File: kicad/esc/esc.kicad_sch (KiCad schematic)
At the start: 33 parts, among them Q1 IRF540N, Q2 IRF540N, Q3 IRF540N, Q4 IRF540N, Q5 IRF540N, Q6 IRF540N, U1 IR2110, U2 IR2110, U3 IR2110

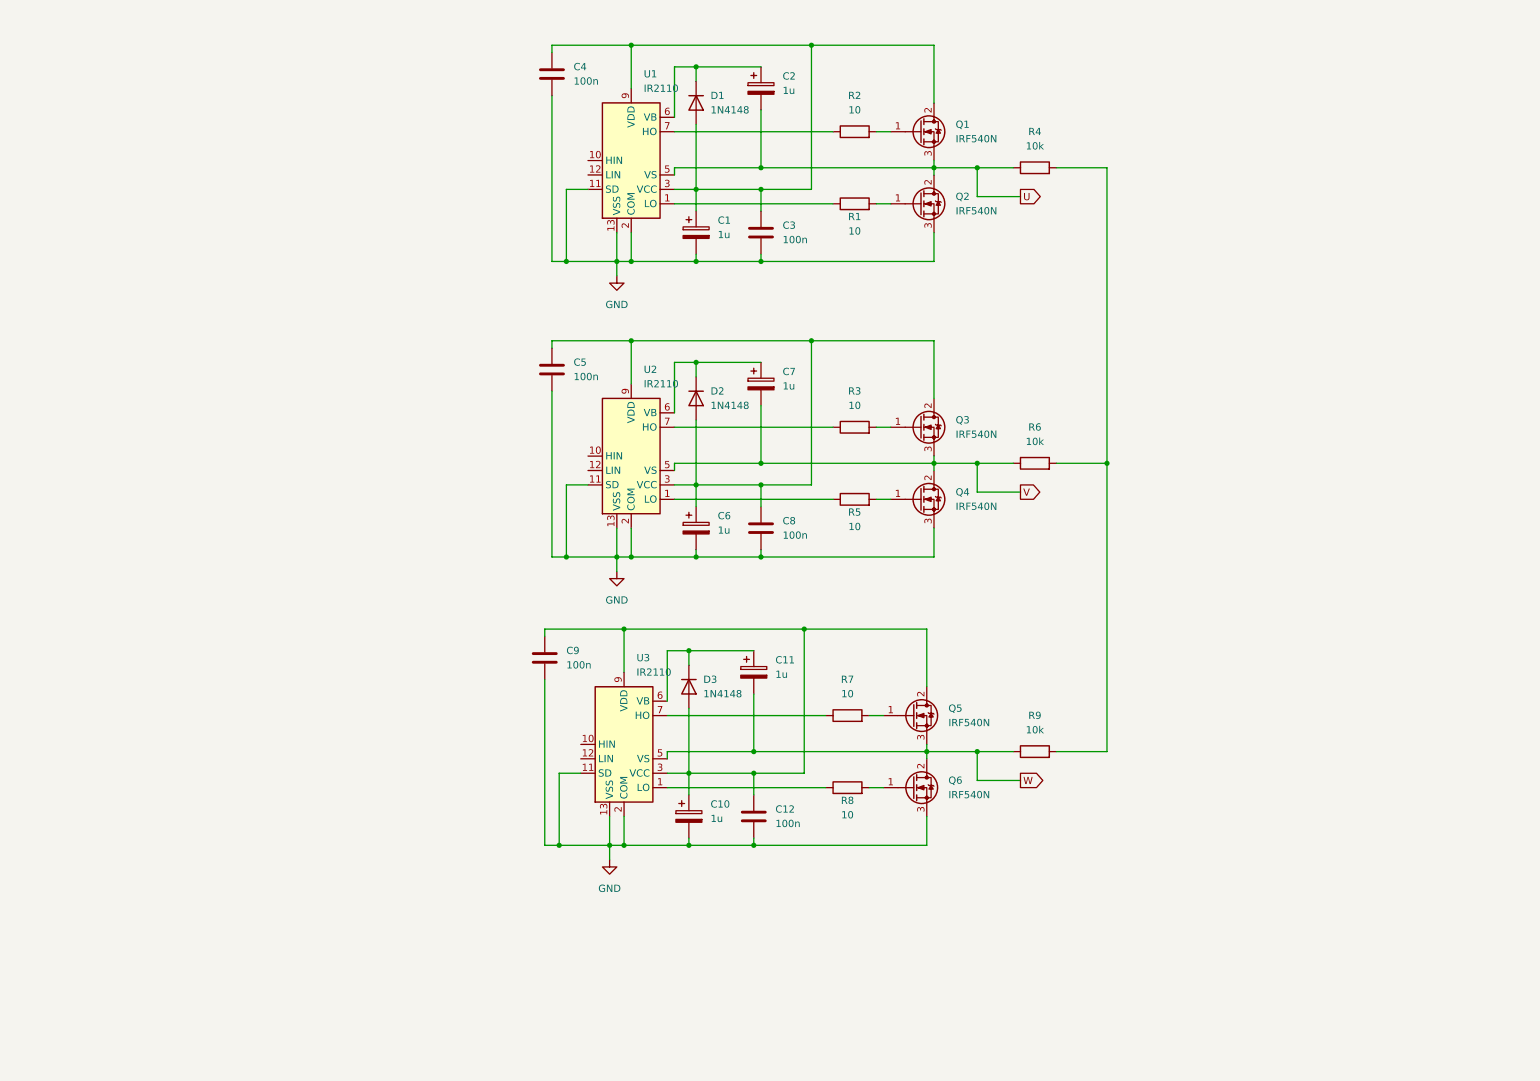
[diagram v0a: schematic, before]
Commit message: Added driver board
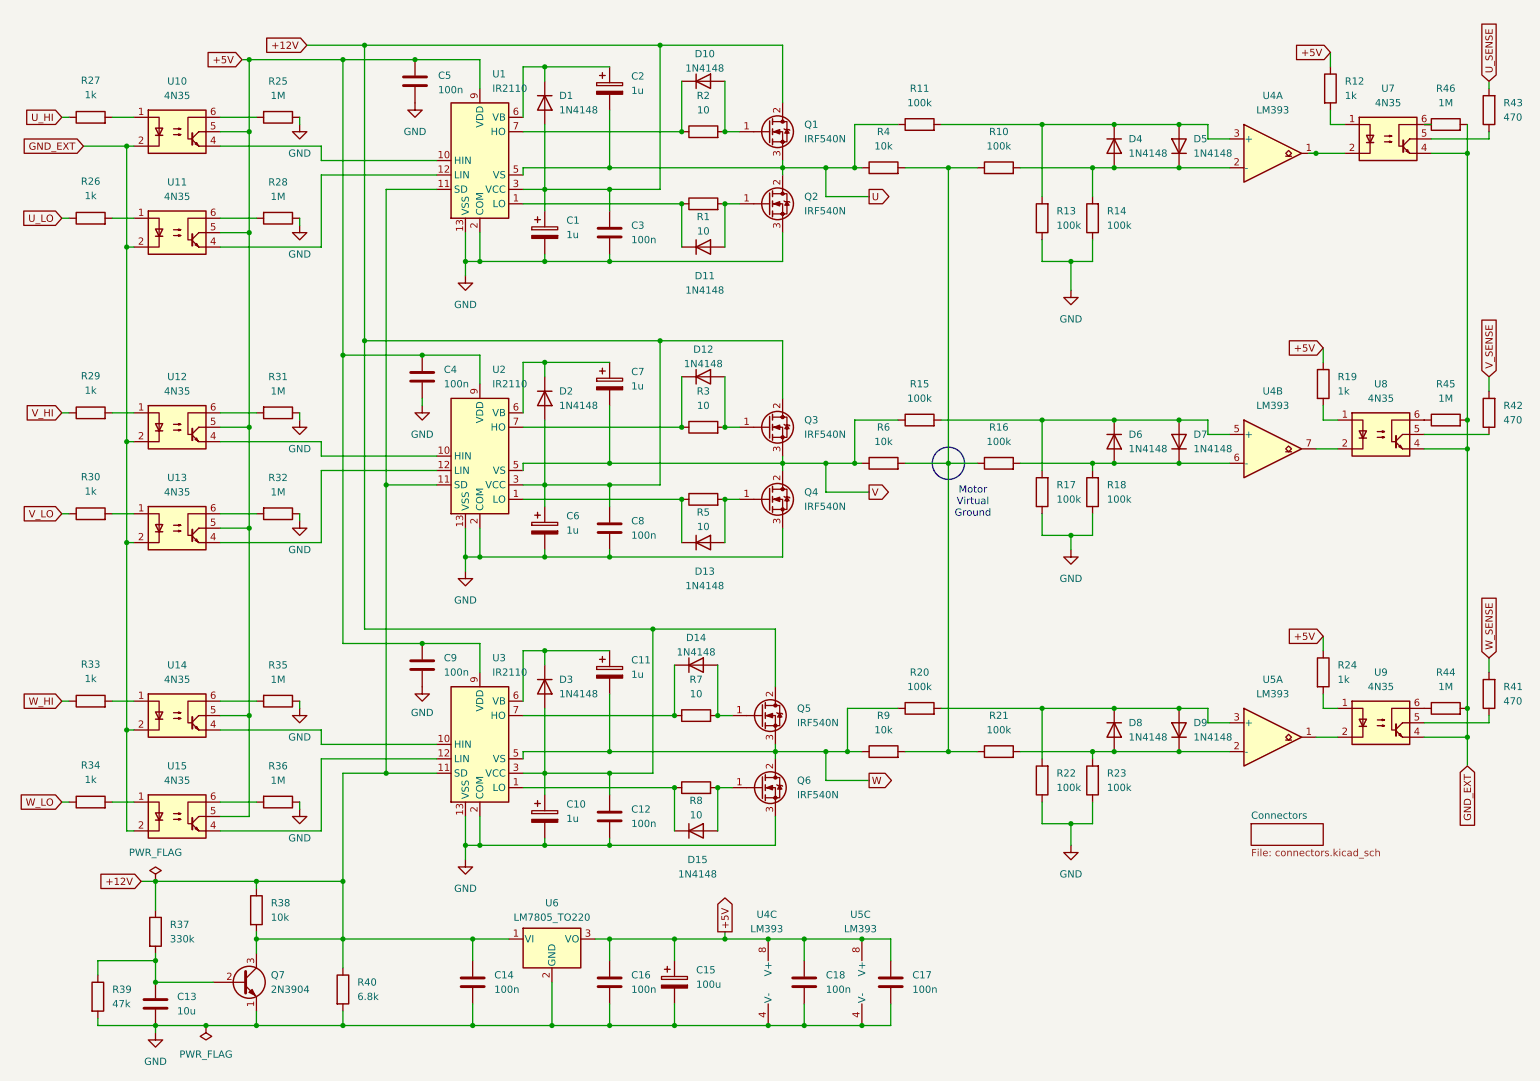
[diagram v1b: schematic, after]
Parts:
- added C13: 10u, symbol Device:C
- added C14, C16, C17, C18: 100n, symbol Device:C
- added C15: 100u, symbol Device:C_Polarized
- added D10, D11, D12, D13, D14, D15, D4, D5, D6, D7, D8, D9: 1N4148, Diode_THT:D_DO-35_SOD27_P7.62mm_Horizontal, symbol Diode:1N4148
- added Q7: 2N3904, Package_TO_SOT_THT:TO-92_Inline, symbol Transistor_BJT:2N3904
- added R10, R11, R13, R14, R15, R16, R17, R18, R20, R21, R22, R23: 100k, Resistor_THT:R_Axial_DIN0207_L6.3mm_D2.5mm_P7.62mm_Horizontal, symbol Device:R
- added R12, R19, R24, R26, R27, R29, R30, R33, R34: 1k, Resistor_THT:R_Axial_DIN0207_L6.3mm_D2.5mm_P7.62mm_Horizontal, symbol Device:R
- added R25, R28, R31, R32, R35, R36, R44, R45, R46: 1M, Resistor_THT:R_Axial_DIN0207_L6.3mm_D2.5mm_P7.62mm_Horizontal, symbol Device:R
- added R37: 330k, Resistor_THT:R_Axial_DIN0207_L6.3mm_D2.5mm_P7.62mm_Horizontal, symbol Device:R
- added R38: 10k, Resistor_THT:R_Axial_DIN0207_L6.3mm_D2.5mm_P7.62mm_Horizontal, symbol Device:R
- added R39: 47k, Resistor_THT:R_Axial_DIN0207_L6.3mm_D2.5mm_P7.62mm_Horizontal, symbol Device:R
- added R40: 6.8k, Resistor_THT:R_Axial_DIN0207_L6.3mm_D2.5mm_P7.62mm_Horizontal, symbol Device:R
- added R41, R42, R43: 470, Resistor_THT:R_Axial_DIN0207_L6.3mm_D2.5mm_P7.62mm_Horizontal, symbol Device:R
- added U10, U11, U12, U13, U14, U15, U7, U8, U9: 4N35, Package_DIP:DIP-6_W7.62mm, symbol Isolator:4N35
- added U4, U5: LM393, Package_DIP:DIP-8_W7.62mm, symbol Comparator:LM393
- added U6: LM7805_TO220, Package_TO_SOT_THT:TO-220-3_Vertical, symbol Regulator_Linear:LM7805_TO220
- R1, R2, R3, R4, R5, R6, R7, R8, R9: footprint (none) -> Resistor_THT:R_Axial_DIN0207_L6.3mm_D2.5mm_P7.62mm_Horizontal
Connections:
- net GND: now also C13.2, C14.2, C15.2, C16.2, C17.2, C18.2, Q7.1 (E), R13.1, R14.1, R17.1, R18.1, R22.1, R23.1, R25.1, R28.1, R31.1, R32.1, R35.1, R36.1, R39.2, R40.2, U4.4 (V-), U5.4 (V-), U6.2 (GND); no longer U1.11 (SD), U2.11 (SD), U3.11 (SD)
- net U: now also R11.1
- net V: now also R15.1
- net W: now also R20.1
- net +12V: now reaches C6.1, C8.1, D2.2 (A), Q3.2 (D), U2.3 (VCC)
- net +12V: now also C1.1, C10.1, C12.1, C3.1, D1.2 (A), D3.2 (A), Q1.2 (D), Q5.2 (D), U1.11 (SD), U1.3 (VCC), U2.11 (SD), U3.11 (SD), U3.3 (VCC), C14.1, Q7.3 (C), R37.1, R38.1, R38.2, R40.1, U6.1 (VI); no longer C5.1, U2.9 (VDD)
- net at R7.1, U3.7 (HO): now also D14.1 (K)
- net at Q5.1 (G), R7.2: now also D14.2 (A)
- net at R4.2, R6.2, R9.2: now also R10.1, R16.1, R21.1
- net at Q1.1 (G), R2.2: now also D10.2 (A)
- net at R5.1, U2.1 (LO): now also D13.1 (K)
- net at Q4.1 (G), R5.2: now also D13.2 (A)
- net at R8.1, U3.1 (LO): now also D15.1 (K)
- net at Q6.1 (G), R8.2: now also D15.2 (A)
- net at R3.1, U2.7 (HO): now also D12.1 (K)
- net at Q3.1 (G), R3.2: now also D12.2 (A)
- net at R1.1, U1.1 (LO): now also D11.1 (K)
- net at U1.10 (HIN): now also U10.4
- net at U1.12 (LIN): now also U11.4
- net at R2.1, U1.7 (HO): now also D10.1 (K)
- net at Q2.1 (G), R1.2: now also D11.2 (A)
- net at U2.10 (HIN): now also U12.4
- net at U2.12 (LIN): now also U13.4
- net at U3.10 (HIN): now also U14.4
- net at U3.12 (LIN): now also U15.4
- new net: R44.1, U9.6
- new net: R30.2, U13.1
- new net: R45.1, U8.6
- new net: D6.1 (K), D7.2 (A), R15.2, R17.2, U4.5 (+)
- new net: D4.1 (K), D5.2 (A), R11.2, R13.2, U4.3 (+)
- new net: R27.2, U10.1
- new net: D6.2 (A), D7.1 (K), R16.2, R18.2, U4.6 (-)
- new net: U4.1, U7.2
- new net: D4.2 (A), D5.1 (K), R10.2, R14.2, U4.2 (-)
- new net: R41.1, U9.5
- new net: R33.2, U14.1
- new net: D8.2 (A), D9.1 (K), R21.2, R23.2, U5.2 (-)
- new net: C13.1, Q7.2 (B), R37.2, R39.1
- new net: R19.2, U8.1
- new net: D8.1 (K), D9.2 (A), R20.2, R22.2, U5.3 (+)
- new net: R42.1, U8.5
- new net: R46.1, U7.6
- new net: R35.2, U14.6
- new net: U4.7, U8.2
- new net: R36.2, U15.6
- new net: R43.1, U7.5
- new net: R32.2, U13.6
- new net: R12.2, U7.1
- new net: R25.2, U10.6
- new net: R24.2, U9.1
- new net: U5.1, U9.2
- new net: R29.2, U12.1
- new net: R26.2, U11.1
- new net: R28.2, U11.6
- new net: R31.2, U12.6
- new net: R34.2, U15.1
- new net +5V: C15.1, C16.1, C17.1, C18.1, C4.1, C5.1, C9.1, R12.1, R19.1, R24.1, U1.9 (VDD), U10.5, U11.5, U12.5, U13.5, U14.5, U15.5, U2.9 (VDD), U3.9 (VDD), U4.8 (V+), U5.8 (V+), U6.3 (VO)
- new net GND_EXT: R44.2, R45.2, R46.2, U10.2, U11.2, U12.2, U13.2, U14.2, U15.2, U7.4, U8.4, U9.4
- new net U_HI: R27.1
- new net U_LO: R26.1
- new net U_SENSE: R43.2
- new net V_HI: R29.1
- new net V_LO: R30.1
- new net V_SENSE: R42.2
- new net W_HI: R33.1
- new net W_LO: R34.1
- new net W_SENSE: R41.2
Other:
- added sheet Connectors (connectors.kicad_sch)
- note added: "Motor Virtual Ground"
- moved on the sheet: C1, C10, C11, C12, C2, C3, C6, C7, C8, D1, D2, D3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
